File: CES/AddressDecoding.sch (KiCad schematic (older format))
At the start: 0 parts

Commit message: Address decoding. Clock. Pannel buttons
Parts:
- added C? (x4): 100nF, symbol Device:C
- added U? (x4): 74LS10, symbol 74xx:74LS10
- added U? (x5): 74LS08, symbol 74xx:74LS08
- added U? (x2): 74LS30, symbol 74xx:74LS30
- added U? (x5): 74HC02, symbol 74xx:74HC02
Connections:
- net labels added: A10, A11, A12, A13, A4, A5, A6, A7, A8, A9, GND, VCC, ~EscMem, ~HabSaiRAM, ~LeRom, ~SelRam
- wire segments 0 -> 89
- no-connect marks 0 -> 5

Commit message: Adding 74HC versions of 74LS chips
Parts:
- removed U? (x4): 74LS10, symbol 74xx:74LS10
- removed U? (x5): 74LS08, symbol 74xx:74LS08
- removed U? (x2): 74LS30, symbol 74xx:74LS30
- added U? (x5): 74HC08, symbol CES:74HC08
- added U? (x4): 74HC10, symbol CES:74HC10
- added U? (x2): 74HC30, symbol CES:74HC30
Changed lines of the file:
@@
 $EndDescr
-$Comp
-L 74xx:74LS10 U?
-U 1 1 610B5E40
-P 3300 2150
-F 0 "U?" H 3300 1950 50  0000 C CNN
-F 1 "74LS10" H 3300 1850 50  0000 C CNN
-F 2 "" H 3300 2150 50  0001 C CNN
-F 3 "http://www.ti.com/lit/gpn/sn74LS10" H 3300 2150 50  0001 C CNN
-	1    3300 2150
-	1    0    0    -1
-$EndComp
-$Comp
-L 74xx:74LS10 U?
-U 4 1 610B8345
-P 4550 6850
-F 0 "U?" H 4600 7200 50  0000 L CNN
-F 1 "74LS10" H 4400 6850 50  0000 L CNN
-F 2 "" H 4550 6850 50  0001 C CNN
-F 3 "http://www.ti.com/lit/gpn/sn74LS10" H 4550 6850 50  0001 C CNN
-	4    4550 6850
-	1    0    0    -1
-$EndComp
-$Comp
-L 74xx:74LS08 U?
-U 2 1 610BAF15
-P 10400 2100
-F 0 "U?" H 10400 2425 50  0000 C CNN
-F 1 "74LS08" H 10400 2334 50  0000 C CNN
-F 2 "" H 10400 2100 50  0001 C CNN
-F 3 "http://www.ti.com/lit/gpn/sn74LS08" H 10400 2100 50  0001 C CNN
-	2    10400 2100
-	1    0    0    -1
-$EndComp
-$Comp
-L 74xx:74LS08 U?
-U 3 1 610BBFF7
-P 10400 2650
-F 0 "U?" H 10400 2975 50  0000 C CNN
-F 1 "74LS08" H 10400 2884 50  0000 C CNN
-F 2 "" H 10400 2650 50  0001 C CNN
-F 3 "http://www.ti.com/lit/gpn/sn74LS08" H 10400 2650 50  0001 C CNN
-	3    10400 2650
-	1    0    0    -1
-$EndComp
-$Comp
-L 74xx:74LS08 U?
-U 4 1 610BD459
-P 10400 1500
-F 0 "U?" H 10400 1825 50  0000 C CNN
-F 1 "74LS08" H 10400 1734 50  0000 C CNN
-F 2 "" H 10400 1500 50  0001 C CNN
-F 3 "http://www.ti.com/lit/gpn/sn74LS08" H 10400 1500 50  0001 C CNN
-	4    10400 1500
-	1    0    0    -1
-$EndComp
-$Comp
-L 74xx:74LS08 U?
-U 5 1 610BE9DE
-P 5000 6850
-F 0 "U?" H 5050 7200 50  0000 L CNN
-F 1 "74LS08" H 4850 6850 50  0000 L CNN
-F 2 "" H 5000 6850 50  0001 C CNN
-F 3 "http://www.ti.com/lit/gpn/sn74LS08" H 5000 6850 50  0001 C CNN
-	5    5000 6850
-	1    0    0    -1
-$EndComp
-$Comp
-L 74xx:74LS30 U?
-U 2 1 610C1D88
-P 5450 6850
-F 0 "U?" H 5500 7200 50  0000 L CNN
-F 1 "74LS30" H 5300 6850 50  0000 L CNN
-F 2 "" H 5450 6850 50  0001 C CNN
-F 3 "http://www.ti.com/lit/gpn/sn74LS30" H 5450 6850 50  0001 C CNN
-	2    5450 6850
-	1    0    0    -1
-$EndComp
 $Comp
 L 74xx:74HC02 U?
@@
 ~SelRam
 $Comp
-L 74xx:74LS08 U?
-U 1 1 610B9FF4
-P 3300 1450
-F 0 "U?" H 3300 1775 50  0000 C CNN
-F 1 "74LS08" H 3300 1684 50  0000 C CNN
-F 2 "" H 3300 1450 50  0001 C CNN
-F 3 "http://www.ti.com/lit/gpn/sn74LS08" H 3300 1450 50  0001 C CNN
-	1    3300 1450
-	1    0    0    -1
-$EndComp
-$Comp
 L 74xx:74HC02 U?
 U 2 1 610C52A5
@@
 	1    0    0    -1
 $EndComp
-$Comp
-L 74xx:74LS10 U?
-U 3 1 610B71E8
-P 10400 3200
-F 0 "U?" H 10400 3525 50  0000 C CNN
-F 1 "74LS10" H 10400 3434 50  0000 C CNN
-F 2 "" H 10400 3200 50  0001 C CNN
-F 3 "http://www.ti.com/lit/gpn/sn74LS10" H 10400 3200 50  0001 C CNN
-	3    10400 3200
-	1    0    0    -1
-$EndComp
 Wire Wire Line
 	5900 6350 5900 6250
@@
 $EndComp
 $Comp
-L 74xx:74LS30 U?
-U 1 1 610C030B
+L CES:74HC08 U?
+U 1 1 608C4157
+P 3300 1450
+F 0 "U?" H 3300 1775 50  0000 C CNN
+F 1 "74HC08" H 3300 1684 50  0000 C CNN
+F 2 "" H 3300 1450 50  0001 C CNN
+F 3 "http://www.ti.com/lit/gpn/sn74HC08" H 3300 1450 50  0001 C CNN
+	1    3300 1450
+	1    0    0    -1
+$EndComp
+$Comp
+L CES:74HC08 U?
+U 5 1 608CB98B
+P 5000 6850
+F 0 "U?" H 5050 7200 50  0000 L CNN
+F 1 "74HC08" H 4850 6850 50  0000 L CNN
+F 2 "" H 5000 6850 50  0001 C CNN
+F 3 "http://www.ti.com/lit/gpn/sn74HC08" H 5000 6850 50  0001 C CNN
+	5    5000 6850
+	1    0    0    -1
+$EndComp
+$Comp
+L CES:74HC08 U?
+U 4 1 608C990A
+P 10400 2650
+F 0 "U?" H 10400 2975 50  0000 C CNN
+F 1 "74HC08" H 10400 2884 50  0000 C CNN
+F 2 "" H 10400 2650 50  0001 C CNN
+F 3 "http://www.ti.com/lit/gpn/sn74HC08" H 10400 2650 50  0001 C CNN
+	4    10400 2650
+	1    0    0    -1
+$EndComp
+$Comp
+L CES:74HC08 U?
+U 3 1 608C7922
+P 10400 2100
+F 0 "U?" H 10400 2425 50  0000 C CNN
+F 1 "74HC08" H 10400 2334 50  0000 C CNN
+F 2 "" H 10400 2100 50  0001 C CNN
+F 3 "http://www.ti.com/lit/gpn/sn74HC08" H 10400 2100 50  0001 C CNN
+	3    10400 2100
+	1    0    0    -1
+$EndComp
+$Comp
+L CES:74HC08 U?
+U 2 1 608C5DDD
+P 10400 1500
+F 0 "U?" H 10400 1825 50  0000 C CNN
+F 1 "74HC08" H 10400 1734 50  0000 C CNN
+F 2 "" H 10400 1500 50  0001 C CNN
+F 3 "http://www.ti.com/lit/gpn/sn74HC08" H 10400 1500 50  0001 C CNN
+	2    10400 1500
+	1    0    0    -1
+$EndComp
+$Comp
+L CES:74HC10 U?
+U 1 1 608E7F40
+P 3300 2150
+F 0 "U?" H 3300 2475 50  0000 C CNN
+F 1 "74HC10" H 3300 2384 50  0000 C CNN
+F 2 "" H 3300 2150 50  0001 C CNN
+F 3 "http://www.ti.com/lit/gpn/sn74HC10" H 3300 2150 50  0001 C CNN
+	1    3300 2150
+	1    0    0    -1
+$EndComp
+$Comp
+L CES:74HC10 U?
+U 2 1 608E8B0D
+P 2050 4300
+F 0 "U?" H 2050 4625 50  0000 C CNN
+F 1 "74HC10" H 2050 4534 50  0000 C CNN
+F 2 "" H 2050 4300 50  0001 C CNN
+F 3 "http://www.ti.com/lit/gpn/sn74HC10" H 2050 4300 50  0001 C CNN
+	2    2050 4300
+	1    0    0    -1
+$EndComp
+$Comp
+L CES:74HC10 U?
+U 3 1 608EA5DE
+P 10400 3200
+F 0 "U?" H 10400 3525 50  0000 C CNN
+F 1 "74HC10" H 10400 3434 50  0000 C CNN
+F 2 "" H 10400 3200 50  0001 C CNN
+F 3 "http://www.ti.com/lit/gpn/sn74HC10" H 10400 3200 50  0001 C CNN
+	3    10400 3200
+	1    0    0    -1
+$EndComp
+$Comp
+L CES:74HC10 U?
+U 4 1 608EBE5C
+P 5450 6850
+F 0 "U?" H 5500 7200 50  0000 L CNN
+F 1 "74HC10" H 5300 6850 50  0000 L CNN
+F 2 "" H 5450 6850 50  0001 C CNN
+F 3 "http://www.ti.com/lit/gpn/sn74HC10" H 5450 6850 50  0001 C CNN
+	4    5450 6850
+	1    0    0    -1
+$EndComp
+$Comp
+L CES:74HC30 U?
+U 1 1 608F4EEB
 P 2050 3250
 F 0 "U?" H 2050 3775 50  0000 C CNN
-F 1 "74LS30" H 2050 3684 50  0000 C CNN
+F 1 "74HC30" H 2050 3684 50  0000 C CNN
 F 2 "" H 2050 3250 50  0001 C CNN
-F 3 "http://www.ti.com/lit/gpn/sn74LS30" H 2050 3250 50  0001 C CNN
+F 3 "http://www.ti.com/lit/gpn/sn74HC30" H 2050 3250 50  0001 C CNN
 	1    2050 3250
 	1    0    0    -1
 $EndComp
 $Comp
-L 74xx:74LS10 U?
-U 2 1 610B6E03
-P 2050 4300
-F 0 "U?" H 2050 4625 50  0000 C CNN
-F 1 "74LS10" H 2050 4534 50  0000 C CNN
-F 2 "" H 2050 4300 50  0001 C CNN
-F 3 "http://www.ti.com/lit/gpn/sn74LS10" H 2050 4300 50  0001 C CNN
-	2    2050 4300
-	1    0    0    -1
-$EndComp
+L CES:74HC30 U?
+U 2 1 608F620B
+P 4550 6850
+F 0 "U?" H 4600 7200 50  0000 L CNN
+F 1 "74HC30" H 4400 6850 50  0000 L CNN
+F 2 "" H 4550 6850 50  0001 C CNN
+F 3 "http://www.ti.com/lit/gpn/sn74HC30" H 4550 6850 50  0001 C CNN
+	2    4550 6850
+	1    0    0    -1
+$EndComp

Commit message: Control Unit
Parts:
- gave numbers to parts that had none: 8
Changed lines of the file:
@@
 $Descr A4 11693 8268
 encoding utf-8
-Sheet 9 16
+Sheet 9 17
 Title "CES"
 Date "2021-04-24"
@@
 $EndDescr
 $Comp
-L 74xx:74HC02 U?
+L 74xx:74HC02 U1001
 U 1 1 610C3622
 P 2050 1350
-F 0 "U?" H 2050 1675 50  0000 C CNN
+F 0 "U1001" H 2050 1675 50  0000 C CNN
 F 1 "74HC02" H 2050 1584 50  0000 C CNN
 F 2 "" H 2050 1350 50  0001 C CNN
@@
 $EndComp
 $Comp
-L 74xx:74HC02 U?
+L 74xx:74HC02 U1001
 U 4 1 610C7DE1
 P 2050 1900
-F 0 "U?" H 2050 2225 50  0000 C CNN
+F 0 "U1001" H 2050 2225 50  0000 C CNN
 F 1 "74HC02" H 2050 2134 50  0000 C CNN
 F 2 "" H 2050 1900 50  0001 C CNN
@@
 $EndComp
 $Comp
-L 74xx:74HC02 U?
+L 74xx:74HC02 U1001
 U 5 1 610C967C
 P 5900 6850
-F 0 "U?" H 6000 7200 50  0000 L CNN
+F 0 "U1001" H 6000 7200 50  0000 L CNN
 F 1 "74HC02" H 5750 6850 50  0000 L CNN
 F 2 "" H 5900 6850 50  0001 C CNN
@@
 $EndComp
 $Comp
-L Device:C C?
+L Device:C C1001
 U 1 1 610CB7A7
 P 3050 6850
-F 0 "C?" H 3100 6950 50  0000 L CNN
+F 0 "C1001" H 3100 6950 50  0000 L CNN
 F 1 "100nF" H 3100 6750 50  0000 L CNN
 F 2 "" H 3088 6700 50  0001 C CNN
@@
 $EndComp
 $Comp
-L Device:C C?
+L Device:C C1002
 U 1 1 610CBFFB
 P 3350 6850
-F 0 "C?" H 3400 6950 50  0000 L CNN
+F 0 "C1002" H 3400 6950 50  0000 L CNN
 F 1 "100nF" H 3400 6750 50  0000 L CNN
 F 2 "" H 3388 6700 50  0001 C CNN
@@
 $EndComp
 $Comp
-L Device:C C?
+L Device:C C1003
 U 1 1 610CC293
 P 3650 6850
-F 0 "C?" H 3700 6950 50  0000 L CNN
+F 0 "C1003" H 3700 6950 50  0000 L CNN
 F 1 "100nF" H 3700 6750 50  0000 L CNN
 F 2 "" H 3688 6700 50  0001 C CNN
@@
 $EndComp
 $Comp
-L Device:C C?
+L Device:C C1004
 U 1 1 610CC594
 P 3950 6850
-F 0 "C?" H 4000 6950 50  0000 L CNN
+F 0 "C1004" H 4000 6950 50  0000 L CNN
 F 1 "100nF" H 4000 6750 50  0000 L CNN
 F 2 "" H 3988 6700 50  0001 C CNN
@@
 NoConn ~ 10700 1500
 $Comp
-L power:GND #PWR?
+L power:GND #PWR01007
 U 1 1 6110F133
 P 10000 1700
-F 0 "#PWR?" H 10000 1450 50  0001 C CNN
+F 0 "#PWR01007" H 10000 1450 50  0001 C CNN
 F 1 "GND" H 10005 1527 50  0000 C CNN
 F 2 "" H 10000 1700 50  0001 C CNN
@@
 	10000 1600 10000 1700
 $Comp
-L power:GND #PWR?
+L power:GND #PWR01006
 U 1 1 61117EEB
 P 10000 1150
-F 0 "#PWR?" H 10000 900 50  0001 C CNN
+F 0 "#PWR01006" H 10000 900 50  0001 C CNN
 F 1 "GND" H 10005 977 50  0000 C CNN
 F 2 "" H 10000 1150 50  0001 C CNN
@@
 NoConn ~ 10700 950
 $Comp
-L power:GND #PWR?
+L power:GND #PWR01008
 U 1 1 61156D0C
 P 10000 2300
-F 0 "#PWR?" H 10000 2050 50  0001 C CNN
+F 0 "#PWR01008" H 10000 2050 50  0001 C CNN
 F 1 "GND" H 10005 2127 50  0000 C CNN
 F 2 "" H 10000 2300 50  0001 C CNN
@@
 	10000 2200 10000 2300
 $Comp
-L power:GND #PWR?
+L power:GND #PWR01009
 U 1 1 61157BC5
 P 10000 2850
-F 0 "#PWR?" H 10000 2600 50  0001 C CNN
+F 0 "#PWR01009" H 10000 2600 50  0001 C CNN
 F 1 "GND" H 10005 2677 50  0000 C CNN
 F 2 "" H 10000 2850 50  0001 C CNN
@@
 	10000 2750 10000 2850
 $Comp
-L power:GND #PWR?
+L power:GND #PWR01010
 U 1 1 61158A9B
 P 10000 3400
-F 0 "#PWR?" H 10000 3150 50  0001 C CNN
+F 0 "#PWR01010" H 10000 3150 50  0001 C CNN
 F 1 "GND" H 10005 3227 50  0000 C CNN
 F 2 "" H 10000 3400 50  0001 C CNN
@@
 ~SelRam
 $Comp
-L 74xx:74HC02 U?
+L 74xx:74HC02 U1001
 U 2 1 610C52A5
 P 10400 950
-F 0 "U?" H 10400 1275 50  0000 C CNN
+F 0 "U1001" H 10400 1275 50  0000 C CNN
 F 1 "74HC02" H 10400 1184 50  0000 C CNN
 F 2 "" H 10400 950 50  0001 C CNN
@@
 	3350 7100 3500 7100
 $Comp
-L power:VCC #PWR?
+L power:VCC #PWR01002
 U 1 1 6119B6D1
 P 3500 6600
-F 0 "#PWR?" H 3500 6450 50  0001 C CNN
+F 0 "#PWR01002" H 3500 6450 50  0001 C CNN
 F 1 "VCC" H 3515 6773 50  0000 C CNN
 F 2 "" H 3500 6600 50  0001 C CNN
@@
 	3500 6600 3650 6600
 $Comp
-L power:VCC #PWR?
+L power:VCC #PWR01004
 U 1 1 6119BBB3
 P 5200 6250
-F 0 "#PWR?" H 5200 6100 50  0001 C CNN
+F 0 "#PWR01004" H 5200 6100 50  0001 C CNN
 F 1 "VCC" H 5215 6423 50  0000 C CNN
 F 2 "" H 5200 6250 50  0001 C CNN
@@
 	5200 6250 5000 6250
 $Comp
-L power:GND #PWR?
+L power:GND #PWR01005
 U 1 1 6119C815
 P 5200 7450
-F 0 "#PWR?" H 5200 7200 50  0001 C CNN
+F 0 "#PWR01005" H 5200 7200 50  0001 C CNN
 F 1 "GND" H 5205 7277 50  0000 C CNN
 F 2 "" H 5200 7450 50  0001 C CNN
@@
 	5200 7450 5450 7450
 $Comp
-L power:GND #PWR?
+L power:GND #PWR01003
 U 1 1 6119D5D7
 P 3500 7100
-F 0 "#PWR?" H 3500 6850 50  0001 C CNN
+F 0 "#PWR01003" H 3500 6850 50  0001 C CNN
 F 1 "GND" H 3505 6927 50  0000 C CNN
 F 2 "" H 3500 7100 50  0001 C CNN
@@
 	800  4400 1750 4400
 $Comp
-L power:VCC #PWR?
+L power:VCC #PWR01001
 U 1 1 6111F1B8
 P 800 4400
-F 0 "#PWR?" H 800 4250 50  0001 C CNN
+F 0 "#PWR01001" H 800 4250 50  0001 C CNN
 F 1 "VCC" H 700 4500 50  0000 C CNN
 F 2 "" H 800 4400 50  0001 C CNN
@@
 A5
 $Comp
-L 74xx:74HC02 U?
+L 74xx:74HC02 U1001
 U 3 1 610C6523
 P 3300 3750
-F 0 "U?" H 3300 4075 50  0000 C CNN
+F 0 "U1001" H 3300 4075 50  0000 C CNN
 F 1 "74HC02" H 3300 3984 50  0000 C CNN
 F 2 "" H 3300 3750 50  0001 C CNN
@@
 $EndComp
 $Comp
-L CES:74HC08 U?
+L CES:74HC08 U1004
 U 1 1 608C4157
 P 3300 1450
-F 0 "U?" H 3300 1775 50  0000 C CNN
+F 0 "U1004" H 3300 1775 50  0000 C CNN
 F 1 "74HC08" H 3300 1684 50  0000 C CNN
 F 2 "" H 3300 1450 50  0001 C CNN
@@
 $EndComp
 $Comp
-L CES:74HC08 U?
+L CES:74HC08 U1004
 U 5 1 608CB98B
 P 5000 6850
-F 0 "U?" H 5050 7200 50  0000 L CNN
+F 0 "U1004" H 5050 7200 50  0000 L CNN
 F 1 "74HC08" H 4850 6850 50  0000 L CNN
 F 2 "" H 5000 6850 50  0001 C CNN
@@
 $EndComp
 $Comp
-L CES:74HC08 U?
+L CES:74HC08 U1004
 U 4 1 608C990A
 P 10400 2650
-F 0 "U?" H 10400 2975 50  0000 C CNN
+F 0 "U1004" H 10400 2975 50  0000 C CNN
 F 1 "74HC08" H 10400 2884 50  0000 C CNN
 F 2 "" H 10400 2650 50  0001 C CNN
@@
 $EndComp
 $Comp
-L CES:74HC08 U?
+L CES:74HC08 U1004
 U 3 1 608C7922
 P 10400 2100
-F 0 "U?" H 10400 2425 50  0000 C CNN
+F 0 "U1004" H 10400 2425 50  0000 C CNN
 F 1 "74HC08" H 10400 2334 50  0000 C CNN
 F 2 "" H 10400 2100 50  0001 C CNN
@@
 $EndComp
 $Comp
-L CES:74HC08 U?
+L CES:74HC08 U1004
 U 2 1 608C5DDD
 P 10400 1500
-F 0 "U?" H 10400 1825 50  0000 C CNN
+F 0 "U1004" H 10400 1825 50  0000 C CNN
 F 1 "74HC08" H 10400 1734 50  0000 C CNN
 F 2 "" H 10400 1500 50  0001 C CNN
@@
 $EndComp
 $Comp
-L CES:74HC10 U?
+L CES:74HC10 U1003
 U 1 1 608E7F40
 P 3300 2150
-F 0 "U?" H 3300 2475 50  0000 C CNN
+F 0 "U1003" H 3300 2475 50  0000 C CNN
 F 1 "74HC10" H 3300 2384 50  0000 C CNN
 F 2 "" H 3300 2150 50  0001 C CNN
@@
 $EndComp
 $Comp
-L CES:74HC10 U?
+L CES:74HC10 U1003
 U 2 1 608E8B0D
 P 2050 4300
-F 0 "U?" H 2050 4625 50  0000 C CNN
+F 0 "U1003" H 2050 4625 50  0000 C CNN
 F 1 "74HC10" H 2050 4534 50  0000 C CNN
 F 2 "" H 2050 4300 50  0001 C CNN
@@
 $EndComp
 $Comp
-L CES:74HC10 U?
+L CES:74HC10 U1003
 U 3 1 608EA5DE
 P 10400 3200
-F 0 "U?" H 10400 3525 50  0000 C CNN
+F 0 "U1003" H 10400 3525 50  0000 C CNN
 F 1 "74HC10" H 10400 3434 50  0000 C CNN
 F 2 "" H 10400 3200 50  0001 C CNN
@@
 $EndComp
 $Comp
-L CES:74HC10 U?
+L CES:74HC10 U1003
 U 4 1 608EBE5C
 P 5450 6850
-F 0 "U?" H 5500 7200 50  0000 L CNN
+F 0 "U1003" H 5500 7200 50  0000 L CNN
 F 1 "74HC10" H 5300 6850 50  0000 L CNN
 F 2 "" H 5450 6850 50  0001 C CNN
@@
 $EndComp
 $Comp
-L CES:74HC30 U?
+L CES:74HC30 U1002
 U 1 1 608F4EEB
 P 2050 3250
-F 0 "U?" H 2050 3775 50  0000 C CNN
+F 0 "U1002" H 2050 3775 50  0000 C CNN
 F 1 "74HC30" H 2050 3684 50  0000 C CNN
 F 2 "" H 2050 3250 50  0001 C CNN
@@
 $EndComp
 $Comp
-L CES:74HC30 U?
+L CES:74HC30 U1002
 U 2 1 608F620B
 P 4550 6850
-F 0 "U?" H 4600 7200 50  0000 L CNN
+F 0 "U1002" H 4600 7200 50  0000 L CNN
 F 1 "74HC30" H 4400 6850 50  0000 L CNN
 F 2 "" H 4550 6850 50  0001 C CNN

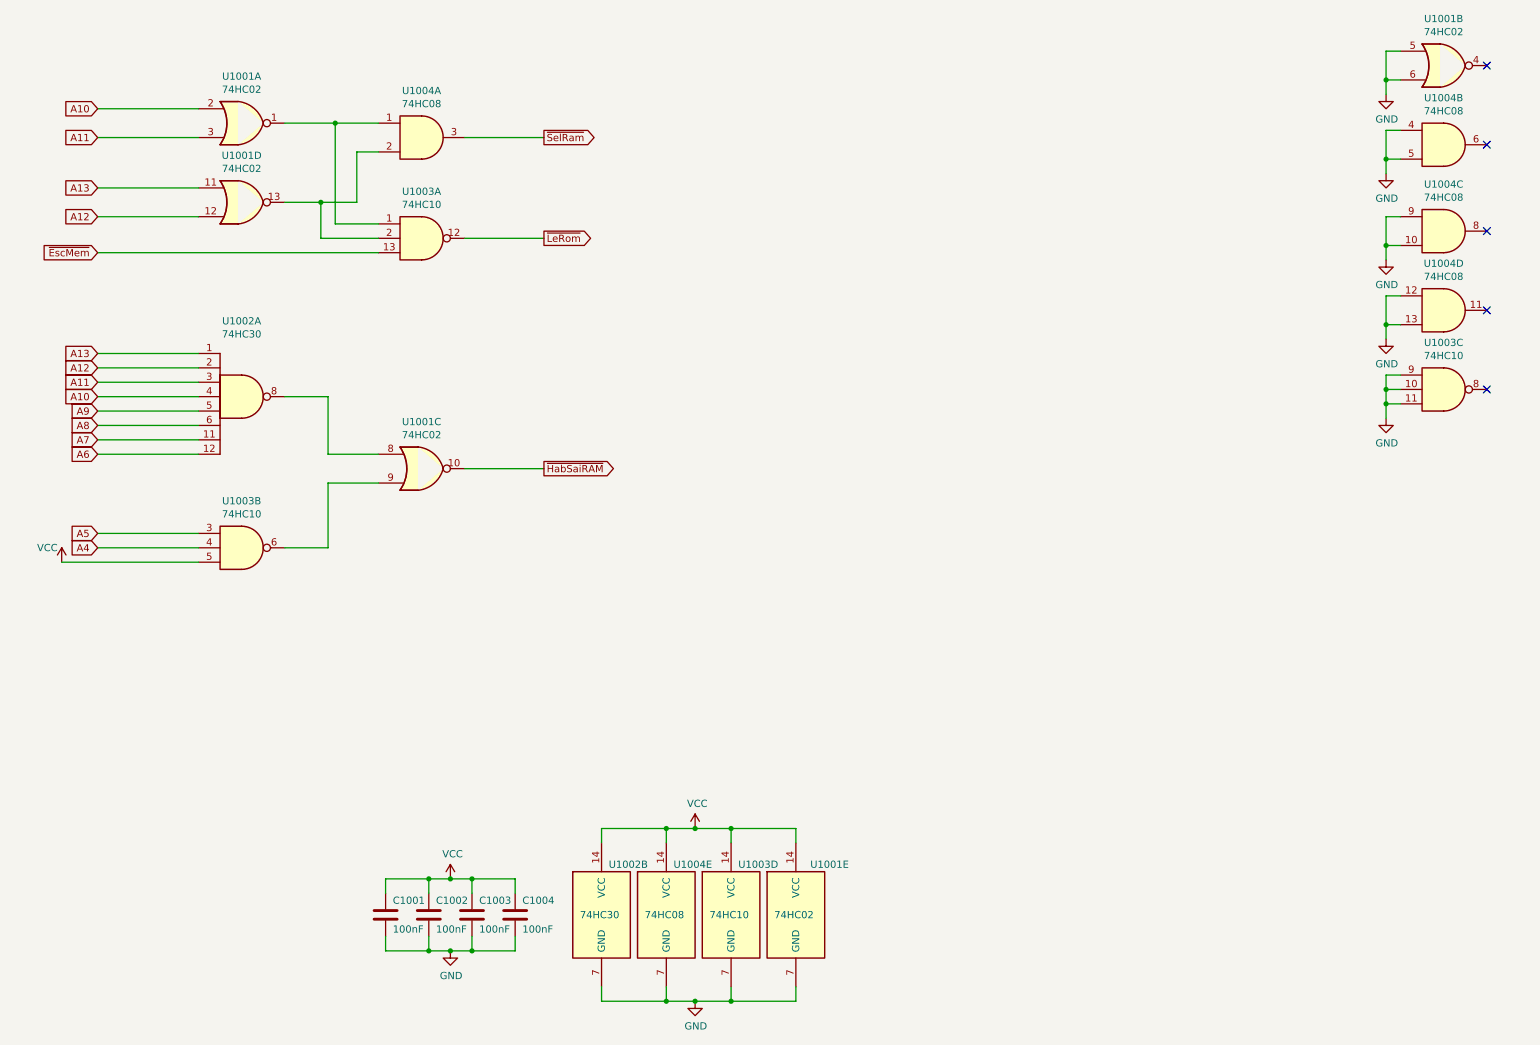
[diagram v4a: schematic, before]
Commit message: Correcting ERC issues
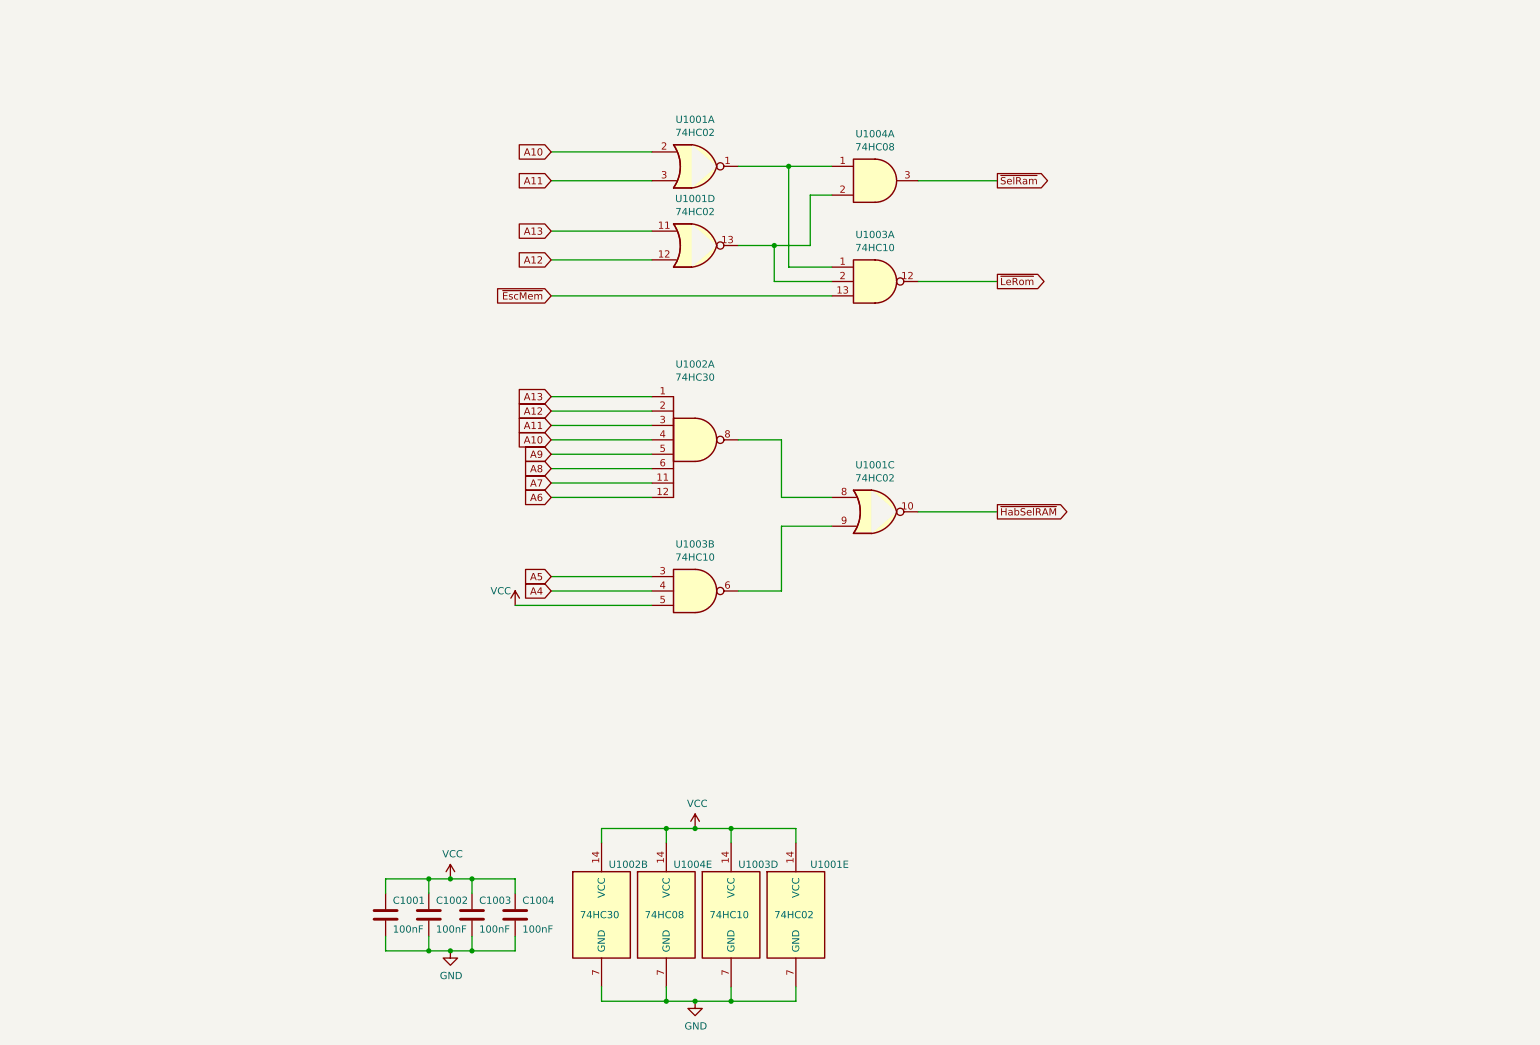
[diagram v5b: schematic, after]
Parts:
- removed unit 2 of U1001
- removed unit 3 of U1003
- removed unit 2 of U1004
- removed unit 3 of U1004
- removed unit 4 of U1004
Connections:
- net ~HabSaiRAM renamed ~HabSelRAM
- no-connect marks 5 -> 0
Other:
- moved on the sheet: U1001A, U1001C, U1001D, U1002A, U1003A, U1003B, U1004A
